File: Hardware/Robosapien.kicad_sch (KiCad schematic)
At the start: 0 parts

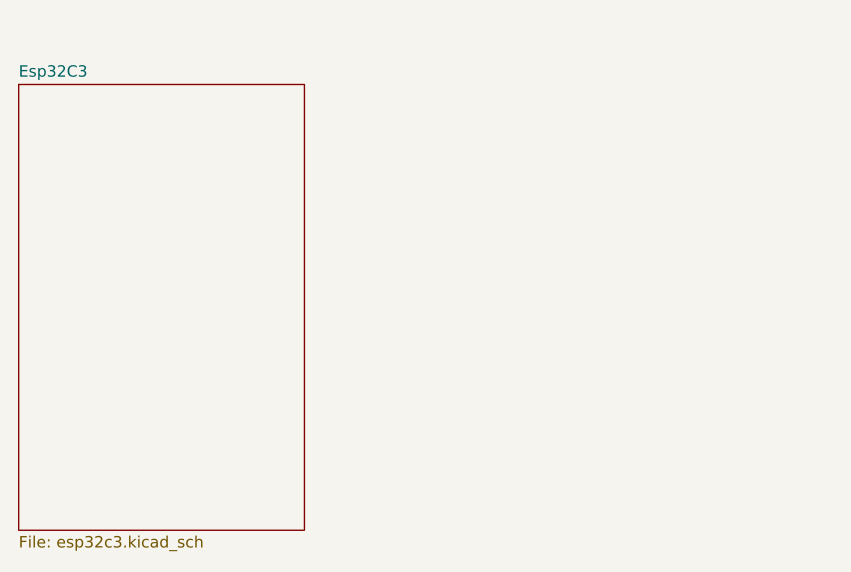
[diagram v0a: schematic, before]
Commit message: Added esp32 and bms
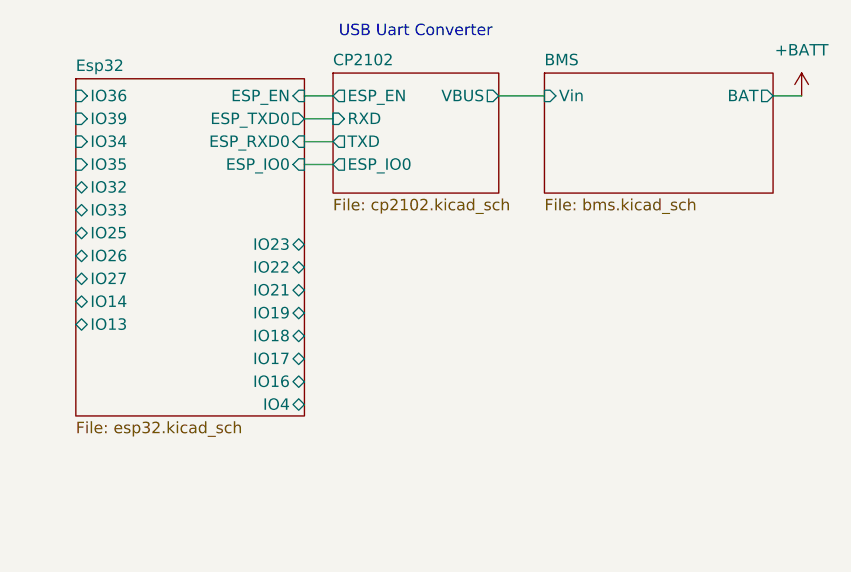
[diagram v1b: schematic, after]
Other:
- sheet Esp32C3 renamed Esp32
- added sheet BMS (bms.kicad_sch)
- added sheet CP2102 (cp2102.kicad_sch)
- sheet Esp32: file esp32c3.kicad_sch -> esp32.kicad_sch
- sheet Esp32 ports: added ESP_EN, ESP_IO0, ESP_RXD0, ESP_TXD0, IO13, IO14, IO16, IO17, IO18, IO19, IO21, IO22, IO23, IO25, IO26, IO27, IO32, IO33, IO34, IO35, IO36, IO39, IO4; removed none
- note added: "USB Uart Converter"

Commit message: New pcb
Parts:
- added CN1, CN2: B2B-PH-K-S(LF)(SN), easyeda2kicad:CONN-TH_B2B-PH-K-S, symbol easyeda2kicad:B2B-PH-K-S(LF)(SN)
- added H1, H2, H3: 9P 2.54 Male Header, easyeda2kicad:HDR-TH_9P-P2.54-V-M, symbol easyeda2kicad:9P 2.54 Male Header
- added H4: 6P 2.54 Male Header, easyeda2kicad:HDR-TH_6P-P2.54-V-M-1, symbol easyeda2kicad:6P 2.54 Male Header
- added R1, R2, R3, R4: 10kΩ 0402 50V, easyeda2kicad:R0402, symbol easyeda2kicad:10kΩ 0402 50V
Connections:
- net +BATT: now also CN2.2, H1.1, H1.2, H1.3, H1.4, H1.5, H1.6, H1.7, H1.8, H1.9, R1.2
- net Esp32/IO36: now also R1.1, R2.2
- new net +3.3V: H4.2, R3.1, R4.1
- new net Audio Amplifier/Speaker+: CN1.2
- new net Audio Amplifier/Speaker-: CN1.1
- new net BMS/BAT-: CN2.1
- new net GND: H2.1, H2.2, H2.3, H2.4, H2.5, H2.6, H2.7, H2.8, H2.9, H4.1, R2.1
- new net SCL: R3.2
- new net SDA: R4.2
- new net SERVO1: H3.1
- new net SERVO2: H3.2
- new net SERVO3: H3.3
- new net SERVO4: H3.4
- new net SERVO5: H3.5
- new net SERVO6: H3.6
- new net SERVO7: H3.7
- new net SERVO8: H3.8
- new net SERVO9: H3.9
- new net Screen1: H4.3
- new net Screen2: H4.4
- new net Screen3: H4.5
- new net Screen4: H4.6
- no-connect marks 0 -> 3
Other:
- added sheet 3.3V Buck Boost (3V3.kicad_sch)
- added sheet Audio Amplifier (audio_amplifier.kicad_sch)
- added sheet Servo Extender (servo_extender.kicad_sch)
- sheet BMS ports: added BAT+, BAT-; removed BAT
- sheet Esp32 ports: added IO2, IO5; removed none
- note added: "Vbat Sensing"

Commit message: V2 Board
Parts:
- added CN3: B2B-PH-K-S(LF)(SN), easyeda2kicad:CONN-TH_B2B-PH-K-S, symbol easyeda2kicad:B2B-PH-K-S(LF)(SN)
- renumbered CN2 to CN1, CN1 to CN2, H3 to H1, H1 to H2, H4 to H3, H2 to H6, R1 to R11, R2 to R12, R3 to R17, R4 to R18
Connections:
- net +BATT: now also CN3.2; no longer CN1.2
- new net BMS/BAT+: CN1.2, CN3.1
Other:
- note added: "On/off Switch"

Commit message: PCB V2
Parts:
- removed H1, H2, H6: 9P 2.54 Male Header, easyeda2kicad:HDR-TH_9P-P2.54-V-M, symbol easyeda2kicad:9P 2.54 Male Header
- removed H3: 6P 2.54 Male Header, easyeda2kicad:HDR-TH_6P-P2.54-V-M-1, symbol easyeda2kicad:6P 2.54 Male Header
- removed R17, R18: 10kΩ 0402 50V, easyeda2kicad:R0402, symbol easyeda2kicad:10kΩ 0402 50V
- added C25, C26: 100nF, easyeda2kicad:C0402_NEW, symbol easyeda2kicad:16V 100nF X7R ±10% 0402
- added R10, R19: 10kΩ 0402 50V, easyeda2kicad:R0402, symbol easyeda2kicad:10kΩ 0402 50V
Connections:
- net Esp32/IO36: now also C26.2
- net Esp32/IO39: now also C25.2, R10.1, R19.2
- net GND: now also C25.1, C26.1, R19.1
- new net VBUS: R10.2
- no-connect marks 3 -> 2
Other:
- removed sheet CP2102
- added sheet Screen Connector (screen.kicad_sch)
- added sheet Servo Connectors (servo.kicad_sch)
- added sheet USB_CP2102 (usb-cp2102.kicad_sch)
- sheet 3.3V Buck Boost ports: added VBat, VUSB; removed Vin
- note added: "Vusb Sensing"
- moved on the sheet: CN1, CN3, R11, R12

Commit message: adsads
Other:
- removed sheet Servo Extender
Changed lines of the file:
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@@
     (effects (font (size 1.27 1.27)) (justify right bottom))
-  )
-  (label "SCL" (at 56.515 142.875 0) (fields_autoplaced)
-    (effects (font (size 1.27 1.27)) (justify left bottom))
   )
   (label "Screen3" (at 36.195 173.355 180) (fields_autoplaced)
@@
   )
   (label "SERVO3" (at 121.285 125.095 0) (fields_autoplaced)
-    (effects (font (size 1.27 1.27)) (justify left bottom))
-  )
-  (label "SDA" (at 56.515 144.907 0) (fields_autoplaced)
     (effects (font (size 1.27 1.27)) (justify left bottom))
   )
@@
         (path "/268ffade-7b22-4f88-a4dd-82181ce0b057"
           (reference "CN1") (unit 1)
-        )
-      )
-    )
-  )
-  (symbol (lib_id "power:+BATT") (at 56.515 138.303 270) (unit 1)
-    (in_bom yes) (on_board yes) (dnp no) (fields_autoplaced)
-    (property "Reference" "#PWR07" (at 52.705 138.303 0)
-      (effects (font (size 1.27 1.27)) hide)
-    )
-    (property "Value" "+BATT" (at 60.579 138.3029 90)
-      (effects (font (size 1.27 1.27)) (justify left))
-    )
-    (property "Footprint" "" (at 56.515 138.303 0)
-      (effects (font (size 1.27 1.27)) hide)
-    )
-    (property "Datasheet" "" (at 56.515 138.303 0)
-      (effects (font (size 1.27 1.27)) hide)
-    )
-    (pin "1")
-    (instances
-      (project "Robosapien"
-        (path "/268ffade-7b22-4f88-a4dd-82181ce0b057"
-          (reference "#PWR07") (unit 1)
         )
       )
@@
       )
     )
-  )
-  (sheet (at 31.623 136.779) (size 24.892 12.192) (fields_autoplaced)
-    (stroke (width 0.1524) (type solid))
-    (fill (color 0 0 0 0.0000))
-    (property "Sheetname" "Servo Extender" (at 31.623 136.0674 0)
-      (effects (font (size 1.27 1.27)) (justify left bottom))
-    )
-    (property "Sheetfile" "servo_extender.kicad_sch" (at 31.623 149.5556 0)
-      (effects (font (size 1.27 1.27)) (justify left top))
-    )
-    (pin "Vin" input (at 56.515 138.303 0)
-      (effects (font (size 1.27 1.27)) (justify right))
-    )
-    (pin "SCL" bidirectional (at 56.515 142.875 0)
-      (effects (font (size 1.27 1.27)) (justify right))
-    )
-    (pin "SDA" bidirectional (at 56.515 144.907 0)
-      (effects (font (size 1.27 1.27)) (justify right))
-    )
-    (instances
-      (project "Robosapien"
-        (path "/268ffade-7b22-4f88-a4dd-82181ce0b057" (page "6"))
-      )
-    )
